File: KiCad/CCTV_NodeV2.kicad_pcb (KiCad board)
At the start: 2 copper layers, 88.4 x 81.8 mm, 9 parts, among them J1 Solar 6V/10W, J2 Battery (ext, 2× 18650 ||), U1 CN3791, U2 TC4056A_BMS, U3 MT3608, U4 ESP32-S3-DevKitC-1 N16R8, U5 OV7670

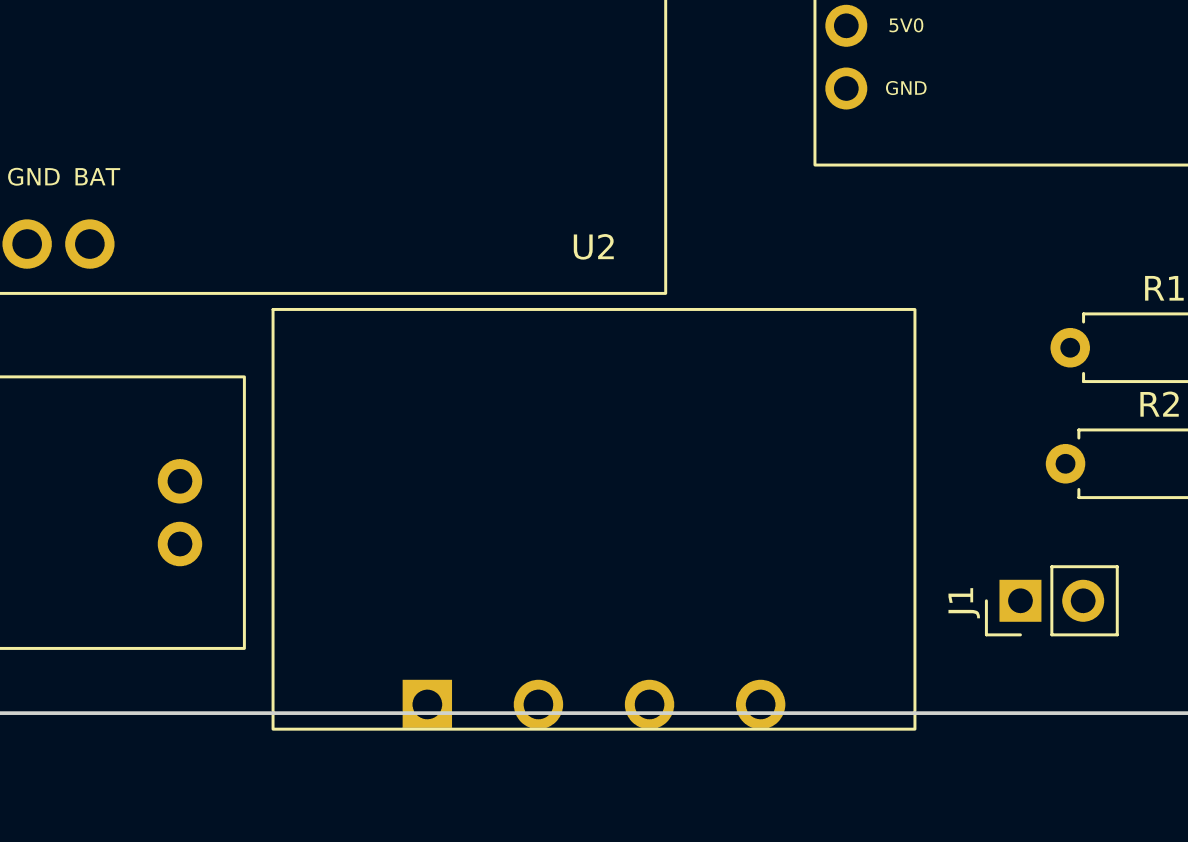
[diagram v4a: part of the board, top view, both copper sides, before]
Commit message: Redesign TC4056A footprint to match actual module (2+4 pad layout)
Physical layout from image:
  LEFT edge : USB-C connector + 2 pads
                pad 1 = IN+  (top, square)
                pad 2 = IN-  (bottom)
  RIGHT edge: 4 pads at 2.54mm pitch
                pad 3 = OUT+ (top)
                pad 4 = B+
                pad 5 = B-
                pad 6 = OUT- (bottom)
  PCB body: 36mm wide x 22mm tall

TC4056A_BMS_Module.kicad_mod:
- Body: (-18,-11) to (+18,+11) = 36x22mm
- USB-C placeholder on left, IC boxes on centre-right
- Left edge pads: 1(IN+,rect,top) at (-17,-5.5), 2(IN-,circ) at (-17,+5.5)
- Right edge pads: 3(OUT+) at (+17,-3.81), 4(B+) at (+17,-1.27),
                   5(B-) at (+17,+1.27),    6(OUT-) at (+17,+3.81)

CCTV_NodeV2.kicad_sch:
- Symbol restored to 6 pins matching pad numbers:
    Pin 1 (IN+)  on left  → NC (no USB connector yet)
    Pin 2 (IN-)  on left  → GND
    Pin 3 (OUT+) on right → P+     ← BATT+ net preserved
    Pin 4 (B+)   on left  → BATT+  ← P+ net preserved
    Pin 5 (B-)   on left  → BATT-  ← BATT- net preserved
    Pin 6 (OUT-) on right → PROT-  ← PROT- net preserved
- Added GND at IN- position (117.3,60.65)
- Added NC at IN+ position (117.3,57.3)

CCTV_NodeV2.kicad_pcb:
- U2 embedded footprint updated with 6-pad layout
- Net assignments: 1=NC, 2=GND, 3=P+, 4=BATT+, 5=BATT-, 6=PROT-
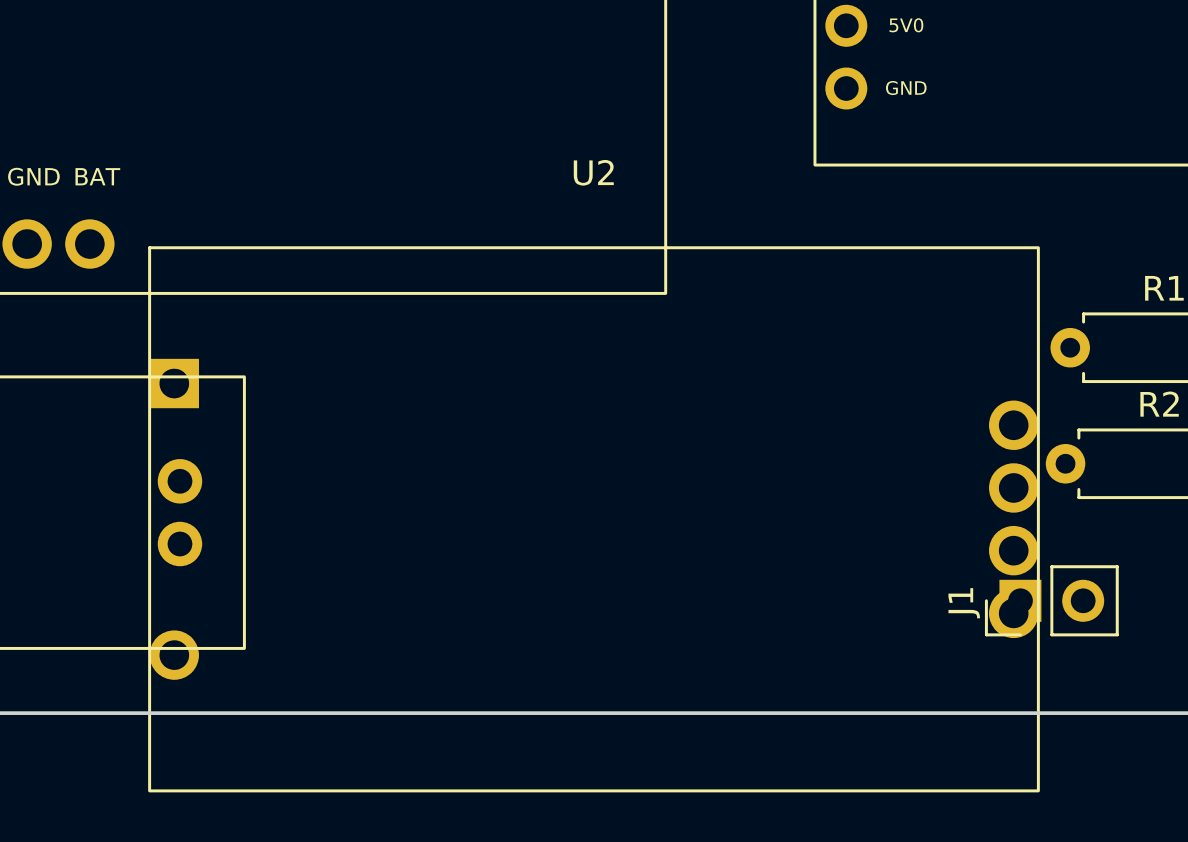
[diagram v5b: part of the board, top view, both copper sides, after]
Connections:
- U2 pad 1: /PROT- -> (no net)
- U2 pad 2: /BATT- -> GND
- U2 pad 3: BATT+ -> /P+
- U2 pad 4: /P+ -> BATT+
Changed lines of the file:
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@@
 		(layer "F.Cu")
 		(at 64.85 107.85)
-		(descr "TC4056A BMS module 26x17mm. USB-C top. 4 pads at BOTTOM EDGE: 1=OUT-/PROT-, 2=B-/BATT-, 3=B+/BATT+, 4=OUT+/P+")
-		(tags "TC4056A TP4056 BMS module USB-C")
+		(descr "TC4056A BMS 36x22mm. USB-C left. Left pads: 1=IN+(top), 2=IN-(bottom). Right pads: 3=OUT+, 4=B+, 5=B-, 6=OUT-")
+		(tags "TC4056A TP4056 BMS USB-C 6pin")
 		(property "Reference" "U2"
-			(at 0 -11 0)
+			(at 0 -14 0)
 			(layer "F.SilkS")
 			(effects (font (size 1 1) (thickness 0.15)))
 		)
 		(property "Value" "TC4056A_BMS"
-			(at 0 11 0)
+			(at 0 14 0)
 			(layer "F.Fab")
 			(effects (font (size 1 1) (thickness 0.15)))
@@
 		(attr through_hole)
 		(duplicate_pad_numbers_are_jumpers no)
-		(fp_rect (start -13 -8.5) (end 13 8.5)
+		(fp_rect (start -18 -11) (end 18 11)
 			(stroke (width 0.12) (type solid)) (fill no)
 			(layer "F.SilkS")
 		)
-		(fp_rect (start -13 -8.5) (end 13 8.5)
+		(fp_rect (start -18 -11) (end 18 11)
 			(stroke (width 0.1) (type solid)) (fill no)
 			(layer "F.Fab")
 		)
-		(fp_rect (start -13.7 -9.2) (end 13.7 9.2)
+		(fp_rect (start -18.7 -11.7) (end 18.7 11.7)
 			(stroke (width 0.05) (type solid)) (fill no)
 			(layer "F.CrtYd")
 		)
-		(fp_rect (start -4 -6) (end 4 -1)
+		(fp_rect (start -16 -4.5) (end -8 4.5)
 			(stroke (width 0.2) (type solid)) (fill no)
 			(layer "F.Fab")
 		)
 		(fp_text user "USB-C"
-			(at 0 -3.5 0) (layer "F.Fab")
+			(at -12 0 0) (layer "F.Fab")
 			(effects (font (size 0.9 0.9) (bold yes) (thickness 0.14)))
 		)
 		(fp_text user "4056A"
-			(at -3 1.75 0) (layer "F.Fab")
+			(at -1 0 0) (layer "F.Fab")
 			(effects (font (size 0.65 0.65) (bold yes) (thickness 0.1)))
 		)
 		(fp_text user "BMS"
-			(at 3.5 1.75 0) (layer "F.Fab")
+			(at 8 0 0) (layer "F.Fab")
 			(effects (font (size 0.65 0.65) (bold yes) (thickness 0.1)))
 		)
 		(pad "1" thru_hole rect
-			(at -6.75 7.5)
+			(at -17 -5.5)
+			(size 2.0 2.0) (drill 1.2)
+			(layers "*.Cu" "*.Mask")
+			(remove_unused_layers no)
+			(uuid "887f1fae-p001-4330-a0da-c1745233d210")
+		)
+		(pad "2" thru_hole circle
+			(at -17 5.5)
+			(size 2.0 2.0) (drill 1.2)
+			(layers "*.Cu" "*.Mask")
+			(remove_unused_layers no)
+			(net "GND")
+			(uuid "887f1fae-p002-4330-a0da-c1745233d210")
+		)
+		(pad "3" thru_hole circle
+			(at 17 -3.81)
+			(size 2.0 2.0) (drill 1.2)
+			(layers "*.Cu" "*.Mask")
+			(remove_unused_layers no)
+			(net "/P+")
+		)
+		(pad "4" thru_hole circle
+			(at 17 -1.27)
+			(size 2.0 2.0) (drill 1.2)
+			(layers "*.Cu" "*.Mask")
+			(remove_unused_layers no)
+			(net "BATT+")
+		)
+		(pad "5" thru_hole circle
+			(at 17 1.27)
+			(size 2.0 2.0) (drill 1.2)
+			(layers "*.Cu" "*.Mask")
+			(remove_unused_layers no)
+			(net "/BATT-")
+		)
+		(pad "6" thru_hole circle
+			(at 17 3.81)
 			(size 2.0 2.0) (drill 1.2)
 			(layers "*.Cu" "*.Mask")
@@
 			(net "/PROT-")
 		)
-		(pad "2" thru_hole circle
-			(at -2.25 7.5)
-			(size 2.0 2.0) (drill 1.2)
-			(layers "*.Cu" "*.Mask")
-			(remove_unused_layers no)
-			(net "/BATT-")
-		)
-		(pad "3" thru_hole circle
-			(at 2.25 7.5)
-			(size 2.0 2.0) (drill 1.2)
-			(layers "*.Cu" "*.Mask")
-			(remove_unused_layers no)
-			(net "BATT+")
-		)
-		(pad "4" thru_hole circle
-			(at 6.75 7.5)
-			(size 2.0 2.0) (drill 1.2)
-			(layers "*.Cu" "*.Mask")
-			(remove_unused_layers no)
-			(net "/P+")
-		)
 		(embedded_fonts no)

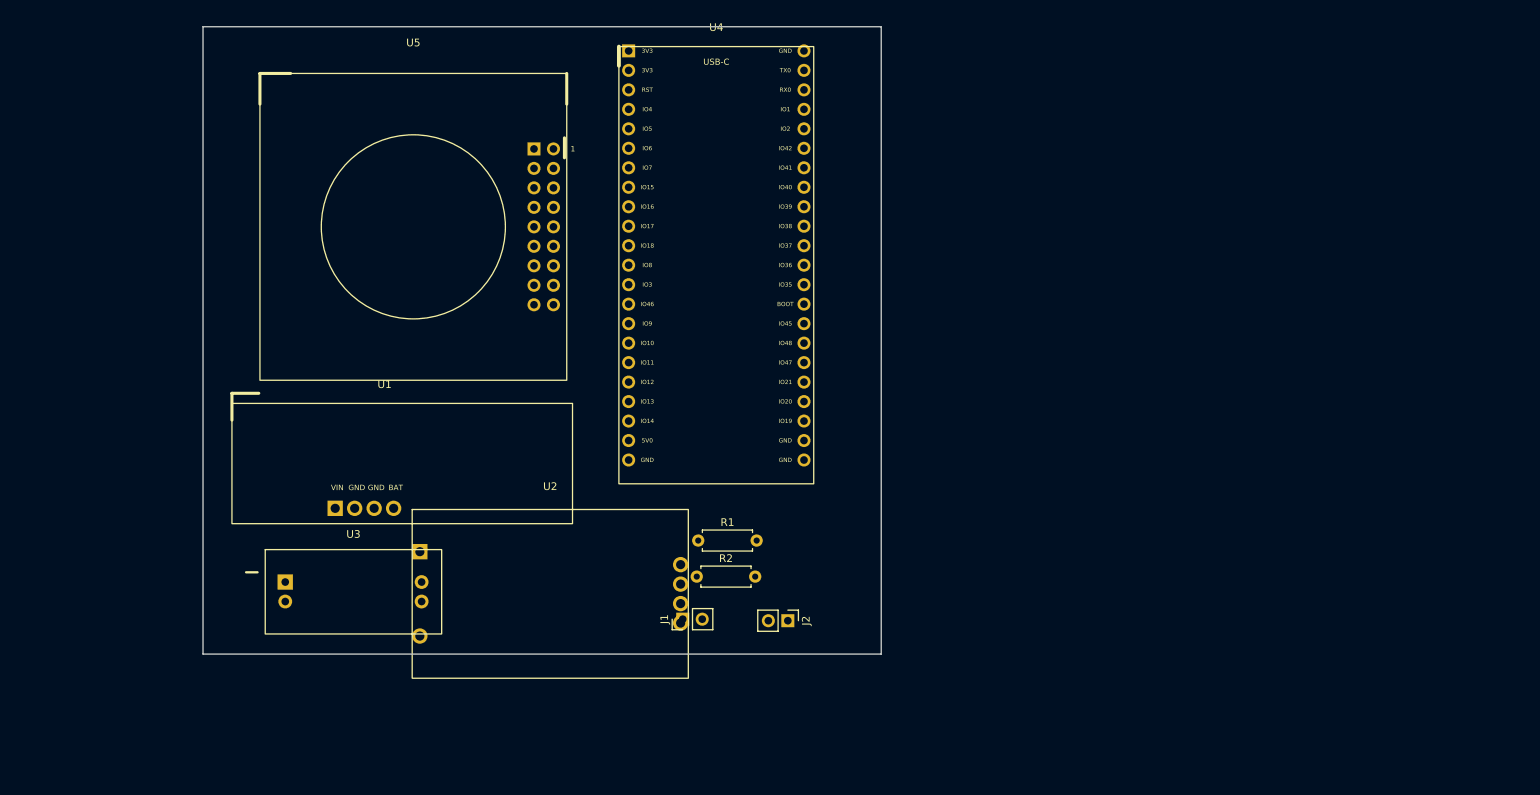
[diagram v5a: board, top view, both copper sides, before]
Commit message: Save PCB and project settings updated by KiCad
KiCad/CCTV_NodeV2.kicad_pcb:
- PCB layout updated by KiCad pcbnew (component positions,
  traces, footprint refreshes after schematic F8 sync)

KiCad/CCTV_NodeV2.kicad_pro:
- Project settings updated by KiCad
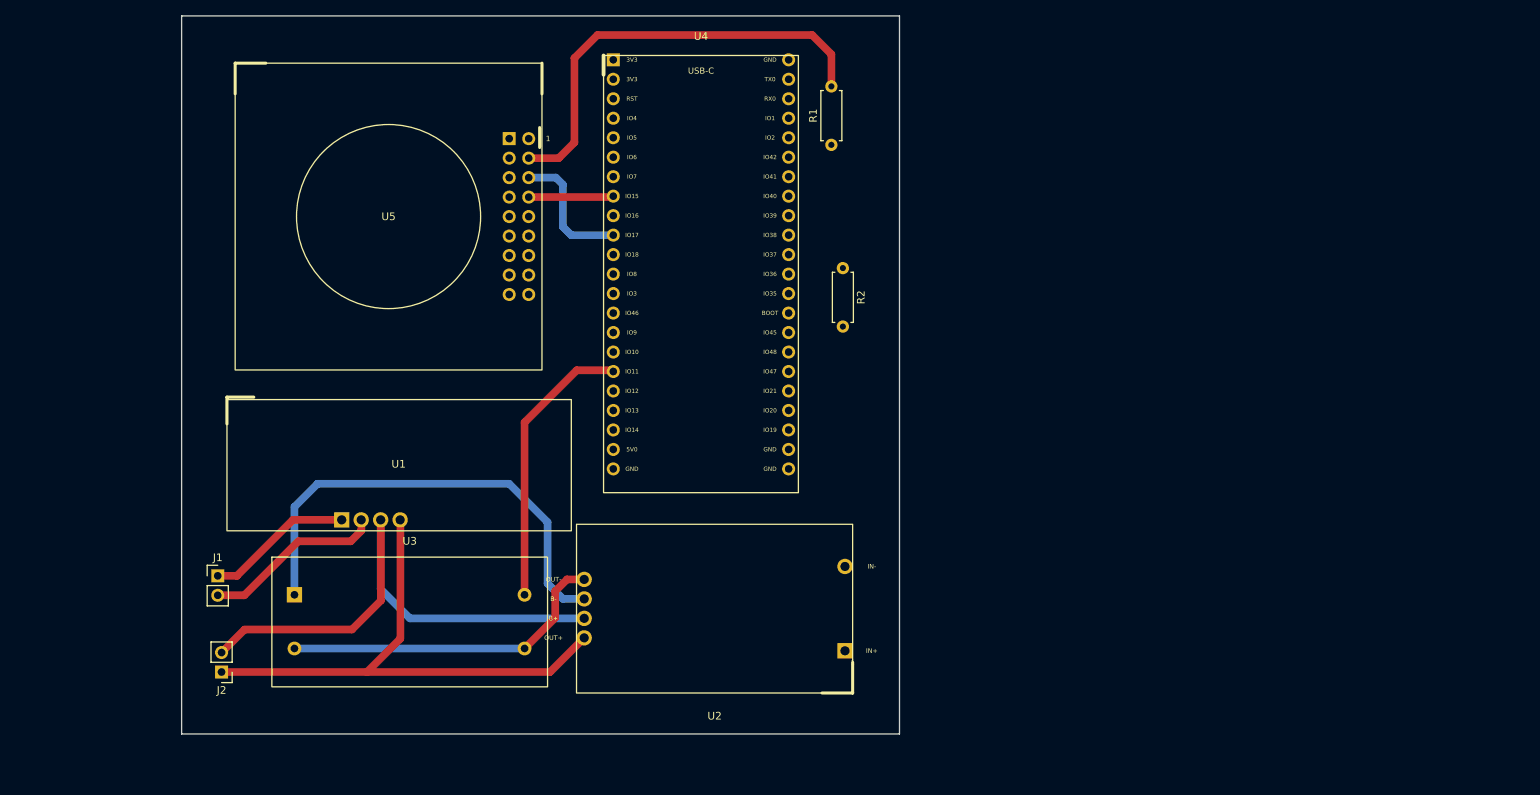
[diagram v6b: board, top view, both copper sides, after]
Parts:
- moved J2 74.1 mm to (22.0, 118.0), turned to 180 degrees
- moved J1 60.9 mm to (21.5, 105.5), turned to 0 degrees
- moved R1 54.4 mm to (101.5, 49.3), turned to 90 degrees
- moved R2 44.5 mm to (103.0, 65.4), turned to -90 degrees
- moved U2 21.5 mm to (86.3, 109.8), turned to 180 degrees
- moved U3 8.28 mm to (46.5, 111.5)
- moved U5 3.50 mm to (60.8, 58.7)
- moved U4 2.31 mm to (84.5, 66.2)
- moved U1 0.82 mm to (40.2, 90.7)
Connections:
- U2 pad 1: (no net) -> unconnected-(U2-IN+-Pad1)
- U2 pad 2: GND -> unconnected-(U2-IN--Pad2)
- U4 pad 1: unconnected-(U4-3V3-Pad1) -> +3V3
- U4 pad 10: /HREF -> unconnected-(U4-GPIO17_D6-Pad10)
- U4 pad 11: /VSYNC -> unconnected-(U4-GPIO18_D5-Pad11)
- U4 pad 12: /SIOC -> unconnected-(U4-GPIO8_D2-Pad12)
- U4 pad 15: +3V3 -> unconnected-(U4-GPIO9_D1-Pad15)
- U4 pad 16: GND -> unconnected-(U4-GPIO10_D3-Pad16)
- U4 pad 17: +5V -> unconnected-(U4-GPIO11_D0-Pad17)
- U4 pad 21: unconnected-(U4-5V-Pad21) -> +5V
- U4 pad 22: unconnected-(U4-GND-Pad22) -> GND
- U4 pad 8: /XCLK -> unconnected-(U4-GPIO15_XCLK-Pad8)
- U4 pad 9: /PCLK -> unconnected-(U4-GPIO16_D7-Pad9)
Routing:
- net /BATT-: track 0.00 -> 71.3 mm
- net BATT+: track 0.00 -> 70.8 mm
- net /P+: track 0.00 -> 61.4 mm
- net /SIOD: track 0.00 -> 57.8 mm
- net /PROT-: track 0.00 -> 43.5 mm
- net +5V: track 0.00 -> 36.9 mm
- net /SOLAR-: track 0.00 -> 23.6 mm
- net /SOLAR+: track 0.00 -> 19.2 mm
- net /HREF: track 0.00 -> 17.4 mm
- net /XCLK: track 0.00 -> 11.1 mm
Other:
- board size 88.4 x 81.8 mm -> 93.6 x 93.6 mm

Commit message: Fix U4 right-column GND pads 23/43/44 net in PCB
PCB had these pads on auto-generated 'unconnected-...' nets
because the schematic GND symbols were added after the last F8 sync.

Updated net assignments directly:
  Pad 23 (GND_R)  : unconnected-(U4-GND_R-Pad23)  → GND
  Pad 43 (GND_R2) : unconnected-(U4-GND_R2-Pad43) → GND
  Pad 44 (GND_R3) : unconnected-(U4-GND_R3-Pad44) → GND

Pad 22 (left col GND) was already GND ✓
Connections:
- U4 pad 23: unconnected-(U4-GND_R-Pad23) -> GND
- U4 pad 43: unconnected-(U4-GND_R2-Pad43) -> GND
- U4 pad 44: unconnected-(U4-GND_R3-Pad44) -> GND
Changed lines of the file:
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@@
 			(layers "*.Cu" "*.Mask")
 			(remove_unused_layers no)
-			(net "unconnected-(U4-GND_R-Pad23)")
+			(net "GND")
 			(pinfunction "GND_R_23")
 			(pintype "no_connect")
@@
 			(layers "*.Cu" "*.Mask")
 			(remove_unused_layers no)
-			(net "unconnected-(U4-GND_R2-Pad43)")
+			(net "GND")
 			(pinfunction "GND_R2_43")
 			(pintype "no_connect")
@@
 			(layers "*.Cu" "*.Mask")
 			(remove_unused_layers no)
-			(net "unconnected-(U4-GND_R3-Pad44)")
+			(net "GND")
 			(pinfunction "GND_R3_44")
 			(pintype "no_connect")
